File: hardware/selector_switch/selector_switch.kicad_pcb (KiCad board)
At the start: 2 copper layers, 26 x 33 mm, 14 parts, among them J1 Conn_01x03_Female, SW1 SW_Rotary12

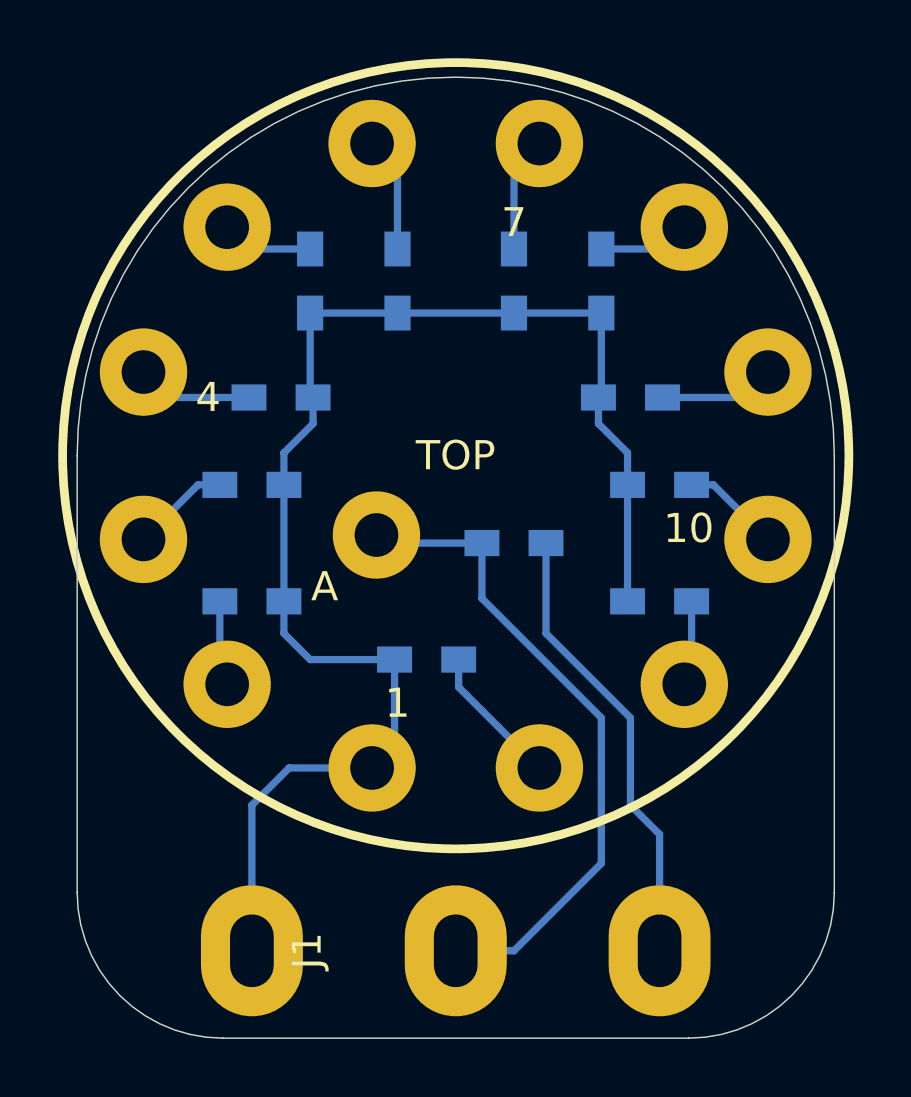
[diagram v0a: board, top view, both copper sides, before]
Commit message: Update synth board to rev3 (fixing volume control) and selector switch to rev2
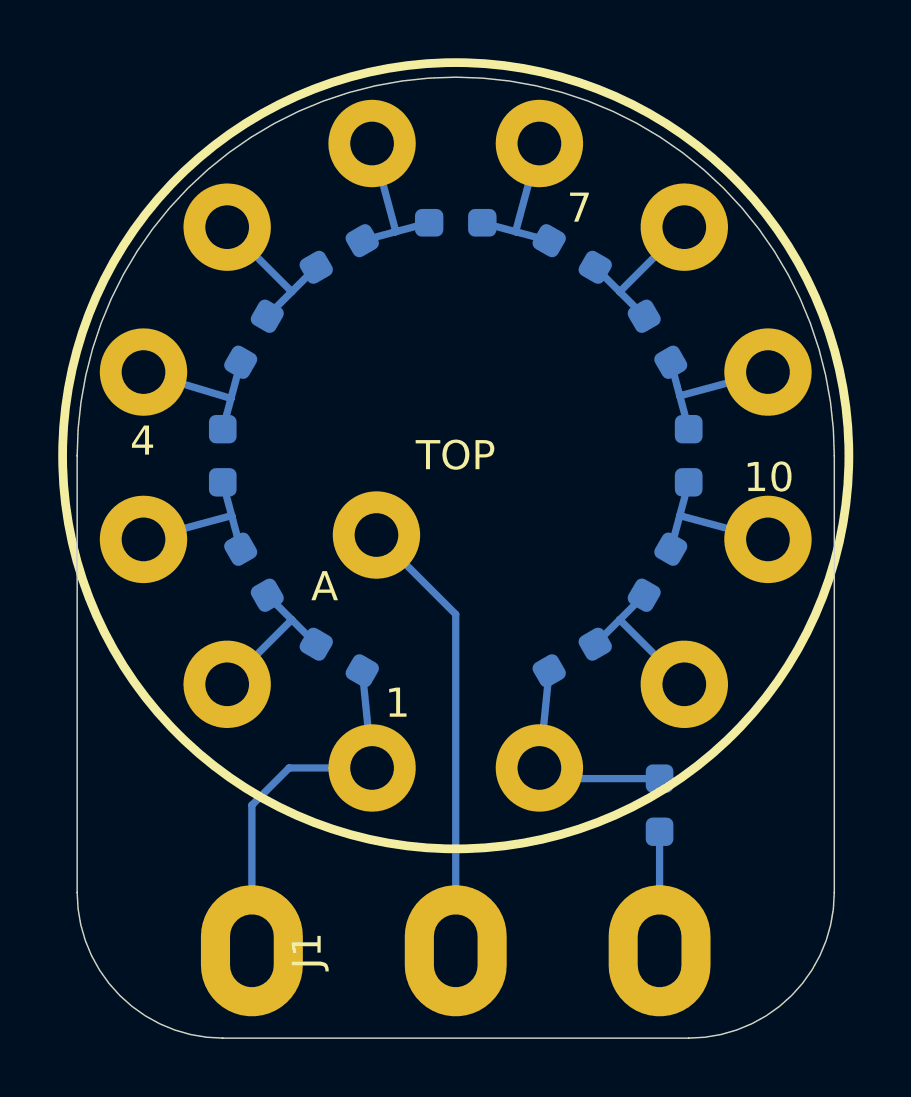
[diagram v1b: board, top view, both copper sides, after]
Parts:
- R1: value 10K -> 12K; footprint Resistors_SMD:R_0603_HandSoldering -> Resistor_SMD:R_0603_1608Metric_Pad0.98x0.95mm_HandSolder
- R10: value 15K -> 3K; footprint Resistors_SMD:R_0603_HandSoldering -> Resistor_SMD:R_0603_1608Metric_Pad0.98x0.95mm_HandSolder
- R11: value 18K -> 3K; footprint Resistors_SMD:R_0603_HandSoldering -> Resistor_SMD:R_0603_1608Metric_Pad0.98x0.95mm_HandSolder
- R12: value 27K -> 3K; footprint Resistors_SMD:R_0603_HandSoldering -> Resistor_SMD:R_0603_1608Metric_Pad0.98x0.95mm_HandSolder
- R2: value 1K -> 3K; footprint Resistors_SMD:R_0603_HandSoldering -> Resistor_SMD:R_0603_1608Metric_Pad0.98x0.95mm_HandSolder
- R3: value 1K8 -> 3K; footprint Resistors_SMD:R_0603_HandSoldering -> Resistor_SMD:R_0603_1608Metric_Pad0.98x0.95mm_HandSolder
- R4: value 2K7 -> 3K; footprint Resistors_SMD:R_0603_HandSoldering -> Resistor_SMD:R_0603_1608Metric_Pad0.98x0.95mm_HandSolder
- R5: value 3K9 -> 3K; footprint Resistors_SMD:R_0603_HandSoldering -> Resistor_SMD:R_0603_1608Metric_Pad0.98x0.95mm_HandSolder
- R6: value 5K6 -> 3K; footprint Resistors_SMD:R_0603_HandSoldering -> Resistor_SMD:R_0603_1608Metric_Pad0.98x0.95mm_HandSolder
- R7: value 6K8 -> 3K; footprint Resistors_SMD:R_0603_HandSoldering -> Resistor_SMD:R_0603_1608Metric_Pad0.98x0.95mm_HandSolder
- R8: value 8K2 -> 3K; footprint Resistors_SMD:R_0603_HandSoldering -> Resistor_SMD:R_0603_1608Metric_Pad0.98x0.95mm_HandSolder
- R9: value 12K -> 3K; footprint Resistors_SMD:R_0603_HandSoldering -> Resistor_SMD:R_0603_1608Metric_Pad0.98x0.95mm_HandSolder
- moved R10 15.0 mm to (147.0, 69.0), turned to -90 degrees
- moved R3 14.2 mm to (161.9, 73.0), turned to 60 degrees
- moved R4 14.1 mm to (163.0, 69.0), turned to 90 degrees
- moved R11 14.0 mm to (148.1, 73.0), turned to -60 degrees
- moved R9 13.1 mm to (148.1, 65.0), turned to -120 degrees
- moved R5 12.1 mm to (161.9, 65.0), turned to 120 degrees
- moved R2 11.2 mm to (159.0, 75.9), turned to 30 degrees
- moved R1 10.3 mm to (162.0, 81.0), turned to 90 degrees
- moved R8 9.05 mm to (151.0, 62.1), turned to -150 degrees
- moved R6 6.07 mm to (159.0, 62.1), turned to 150 degrees
- moved R12 3.00 mm to (151.0, 75.9), turned to -30 degrees
- moved R7 2.83 mm to (155.0, 61.0), turned to 180 degrees
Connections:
- net VCC renamed Net-(J1-Pad3)
- J1 pad 1: GND -> Net-(J1-Pad1)
- R1 pad 2: /OUT -> Net-(R1-Pad2)
- R10 pad 1: GND -> Net-(R10-Pad1)
- R11 pad 1: GND -> Net-(R10-Pad2)
- R12 pad 1: GND -> Net-(R11-Pad2)
- R12 pad 2: Net-(R12-Pad2) -> Net-(J1-Pad1)
- R2 pad 1: GND -> Net-(R1-Pad2)
- R3 pad 1: GND -> Net-(R2-Pad2)
- R4 pad 1: GND -> Net-(R3-Pad2)
- R5 pad 1: GND -> Net-(R4-Pad2)
- R6 pad 1: GND -> Net-(R5-Pad2)
- R7 pad 1: GND -> Net-(R6-Pad2)
- R8 pad 1: GND -> Net-(R7-Pad2)
- R9 pad 1: GND -> Net-(R8-Pad2)
- R9 pad 2: Net-(R9-Pad2) -> Net-(R10-Pad1)
- SW1 pad 1: GND -> Net-(J1-Pad1)
- SW1 pad 10: Net-(R10-Pad2) -> Net-(R3-Pad2)
- SW1 pad 11: Net-(R11-Pad2) -> Net-(R2-Pad2)
- SW1 pad 12: Net-(R12-Pad2) -> Net-(R1-Pad2)
- SW1 pad 2: Net-(R2-Pad2) -> Net-(R11-Pad2)
- SW1 pad 3: Net-(R3-Pad2) -> Net-(R10-Pad2)
- SW1 pad 4: Net-(R4-Pad2) -> Net-(R10-Pad1)
- SW1 pad 5: Net-(R5-Pad2) -> Net-(R8-Pad2)
- SW1 pad 6: Net-(R6-Pad2) -> Net-(R7-Pad2)
- SW1 pad 7: Net-(R7-Pad2) -> Net-(R6-Pad2)
- SW1 pad 8: Net-(R8-Pad2) -> Net-(R5-Pad2)
- SW1 pad 9: Net-(R9-Pad2) -> Net-(R4-Pad2)
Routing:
- net GND: track 49.9 -> 0.00 mm
- net Net-(J1-Pad1): track 0.00 -> 13.0 mm
- net Net-(J1-Pad3): track 15.6 -> 4.09 mm
- net Net-(R1-Pad2): track 0.00 -> 7.63 mm
- net /OUT: track 22.7 -> 15.4 mm
- net Net-(R10-Pad1): track 0.00 -> 5.52 mm
- net Net-(R12-Pad2): track 4.87 -> 0.00 mm
- net Net-(R9-Pad2): track 3.98 -> 0.00 mm
- net Net-(R2-Pad2): track 2.95 -> 5.51 mm
- net Net-(R11-Pad2): track 2.95 -> 5.51 mm
- net Net-(R5-Pad2): track 3.06 -> 5.51 mm
- net Net-(R8-Pad2): track 3.16 -> 5.51 mm
- net Net-(R10-Pad2): track 3.40 -> 5.51 mm
- net Net-(R3-Pad2): track 3.40 -> 5.51 mm
- net Net-(R7-Pad2): track 3.98 -> 5.51 mm
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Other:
- net class Default removed
